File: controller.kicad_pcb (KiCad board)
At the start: 2 copper layers, 57 x 122 mm, 150 parts, among them J1 KYCON_KPJX-4S-S, J10 MicroFit_2x04, J11 JST_S4B-XH, J12 MicroFit_2x04, J13 JST_B2B-XH, J14 JST_S2B-XH, J16 MLX_1x03, J17 MLX_1x03, J2 MicroFit_2x02, J3 24V/5A OUT, J4 DB25 FEMALE, J5 JST_S6B-XH, J6 JST_S4B-XH, J7 MicroFit_2x04, J8 JST_S4B-XH, J9 JST_S4B-XH, K1 TE_OJS_24V_10A, Q1 BC847, Q2 IRF9540SPBF, Q3 BC857, Q4 BC847, Q5 BC857, U1 MC78M12CDT-TR, U2 MAX5035BUSA, U3 LM358EDR2G, U4 74HC245, U5 74HC245, U6 ACSL-6310, U7 ACSL-6310

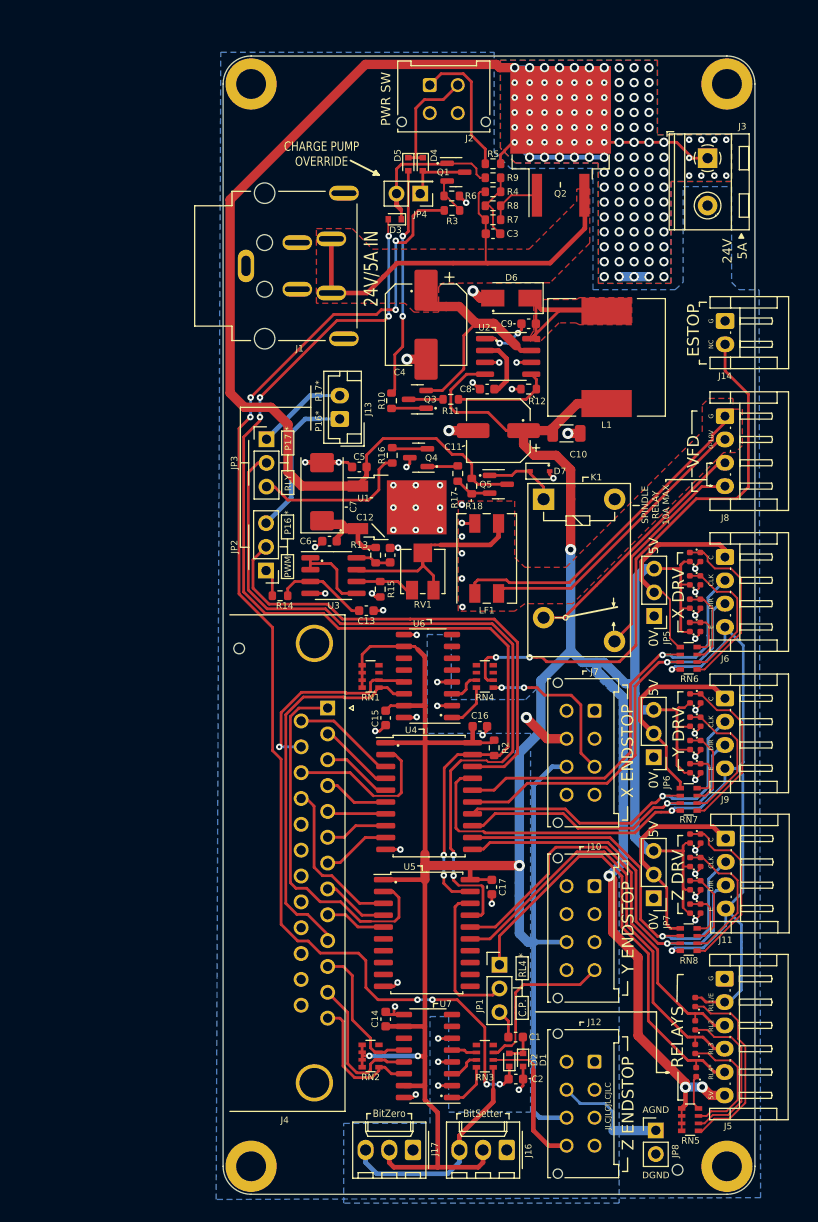
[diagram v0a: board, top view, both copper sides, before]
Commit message: Fixed yesterday's fix. Changed relay layout to allow 3A max terminal current, actually. Also changed VFD 0-10V PCB Farraday shield to reference VFD AGND instead of local GND.
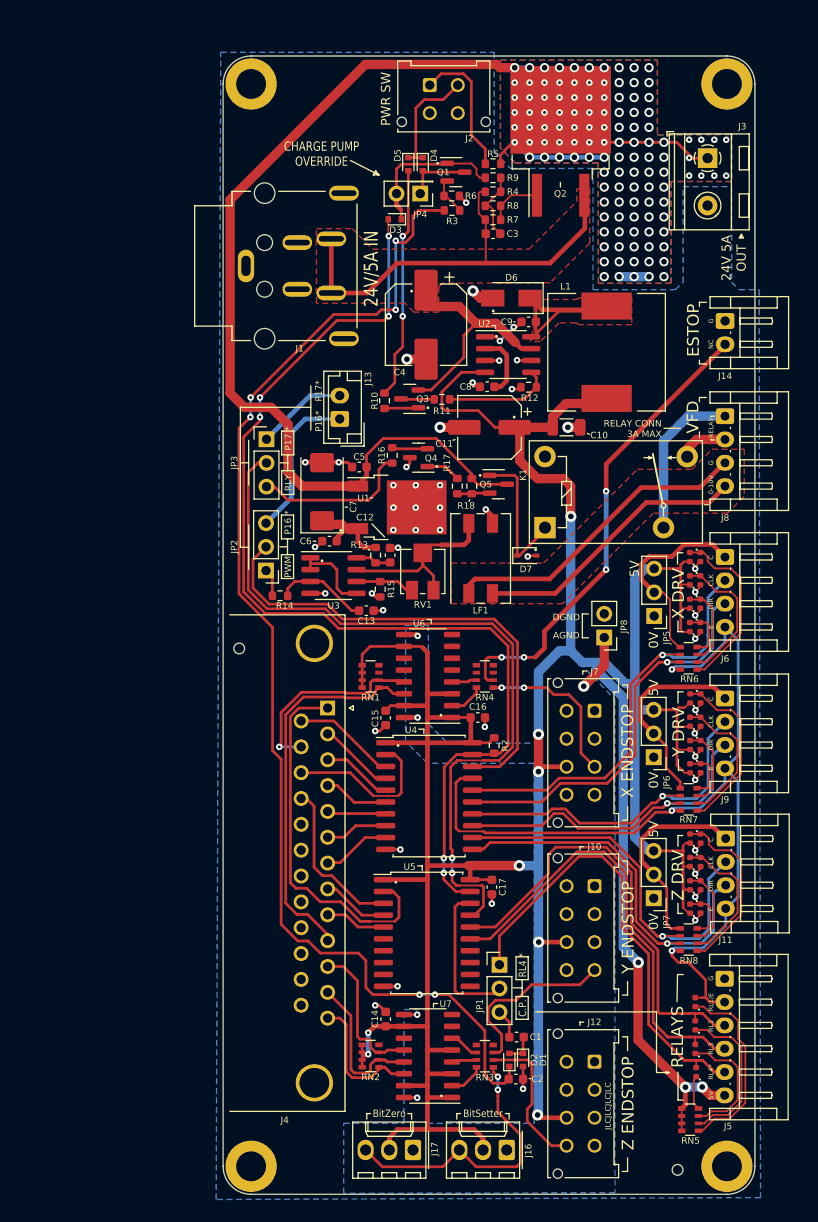
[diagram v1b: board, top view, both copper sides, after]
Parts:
- removed NT24: DNI, -Project:NetTie-2_SMD_Pad1.0mm
- K1: value TE_OJS_24V_10A -> OJS-SH-124HMF
- NT21: footprint -Project:NetTie-2_SMD_Pad0.3mm -> -Project:NetTie-2_SMD_Pad1.0mm; moved to B.Cu
- NT22: footprint -Project:NetTie-2_SMD_Pad0.3mm -> -Project:NetTie-2_SMD_Pad1.0mm
- NT23: footprint -Project:NetTie-2_SMD_Pad0.3mm -> -Project:NetTie-2_SMD_Pad0.5mm
- NT7: moved to F.Cu
- moved JP8 53.1 mm to (117.4, 111.3), turned to 180 degrees
- moved NT22 19.1 mm to (128.0, 90.1), turned to 0 degrees
- moved D7 9.16 mm to (109.1, 102.5)
- moved NT7 6.71 mm to (125.7, 146.2), turned to 0 degrees
- moved NT10 6.49 mm to (113.8, 148.6), turned to 0 degrees
- moved NT21 5.22 mm to (123.8, 96.8), turned to 90 degrees
- moved K1 3.05 mm to (111.0, 99.5), turned to 0 degrees
- moved R17 1.35 mm to (101.7, 95.1)
- moved NT12 1.35 mm to (106.0, 160.8)
- moved C11 1.01 mm to (105.1, 88.8)
- moved C16 0.97 mm to (103.8, 119.9)
- moved R11 0.95 mm to (100.0, 85.8)
- moved Q3 0.82 mm to (96.5, 85.8)
- moved NT13 0.75 mm to (109.7, 113.5)
- moved R10 0.75 mm to (93.8, 86.0)
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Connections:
- J10 pad 7: Net-(J10-Pad7) -> +5V
- J12 pad 7: Net-(J10-Pad7) -> +5V
- J7 pad 7: Net-(J10-Pad7) -> +5V
- J8 pad 1: /Connectors/DGND -> /Connectors/VFD_FWD
- J8 pad 2: /Connectors/0-10V -> /Connectors/VFD_XGND
- J8 pad 3: /Connectors/XGND -> /Connectors/VFD_0-10V
- J8 pad 4: /Connectors/FWD -> /Connectors/VFD_AGND
- K1 pad 3: /Connectors/SPNDL_RELAY_NO -> /Connectors/SPNDL_RELAY_COM
- K1 pad 5: /Connectors/SPNDL_RELAY_COM -> /Connectors/SPNDL_RELAY_NO
- LF1 pad 1: /Connectors/DGND -> /Connectors/VFD_0-10V
- LF1 pad 2: /Connectors/0-10V -> /Connectors/VFD_AGND
- LF1 pad 3: Net-(LF1-Pad3) -> GND
- LF1 pad 4: GND -> Net-(LF1-Pad4)
- NT21 pad 2: /Connectors/FWD -> /Connectors/VFD_FWD
- NT22 pad 2: /Connectors/XGND -> /Connectors/VFD_XGND
- NT23 pad 2: Net-(LF1-Pad3) -> Net-(LF1-Pad4)
- RN3 pad 2: Net-(RN3-Pad2) -> Net-(U7-Pad6)
- RN3 pad 3: Net-(RN3-Pad3) -> Net-(U7-Pad4)
- U6 pad 1: Net-(RN4-Pad8) -> +5V
- U6 pad 16: GND -> GNDA
- U6 pad 2: GNDA -> Net-(RN4-Pad8)
- U6 pad 3: Net-(RN4-Pad7) -> +5V
- U6 pad 4: GNDA -> Net-(RN4-Pad7)
- U6 pad 9: GND -> GNDA
- U7 pad 1: Net-(RN3-Pad4) -> +5V
- U7 pad 16: GND -> GNDA
- U7 pad 2: GNDA -> Net-(RN3-Pad4)
- U7 pad 3: Net-(RN3-Pad3) -> +5V
- U7 pad 4: GNDA -> Net-(U7-Pad4)
- U7 pad 5: Net-(RN3-Pad2) -> +5V
- U7 pad 6: GNDA -> Net-(U7-Pad6)
- U7 pad 9: GND -> GNDA
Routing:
- net Net-(J10-Pad7): track 52.6 -> 0.00 mm
- net +5V: track 181.3 -> 229.0 mm, vias 4 -> 8
- net /Connectors/DGND: track 35.6 -> 0.00 mm
- net /Connectors/VFD_0-10V: track 0.00 -> 33.8 mm
- net /Connectors/0-10V: track 30.6 -> 0.00 mm
- net /Connectors/VFD_AGND: track 0.00 -> 29.7 mm
- net /Connectors/SPNDL_RELAY_NO: track 21.0 -> 2.05 mm
- net /Connectors/XGND: track 18.0 -> 0.00 mm
- net /Connectors/VFD_FWD: track 0.00 -> 13.5 mm
- net GNDA: track 25.5 -> 12.0 mm, vias 6 -> 5
- net /Connectors/EMRG_STOP: track 51.8 -> 42.0 mm, vias 0 -> 2
- net /Connectors/YMIN_OUT: track 5.94 -> 15.7 mm
- net /Connectors/YMIN: track 11.0 -> 2.91 mm
- net Net-(LF1-Pad3): track 8.01 -> 0.00 mm
- net Net-(D7-Pad1): track 8.12 -> 15.8 mm
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- added copper zone on F.Cu, net /Connectors/VFD_AGND
- removed copper zone on F.Cu, net GND
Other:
- board text added: "24V 5A OUT"
- board text added: "Farraday shield"
- board text added: "RELAY"
- board text added: "RELAY CONN 3A MAX"
- board text removed: "24V 5A"
- board text removed: "SPINDLE RELAY 10A MAX"

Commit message: Tidied up F.Fab and some silk screen. Added back 2 missing tooling holes.
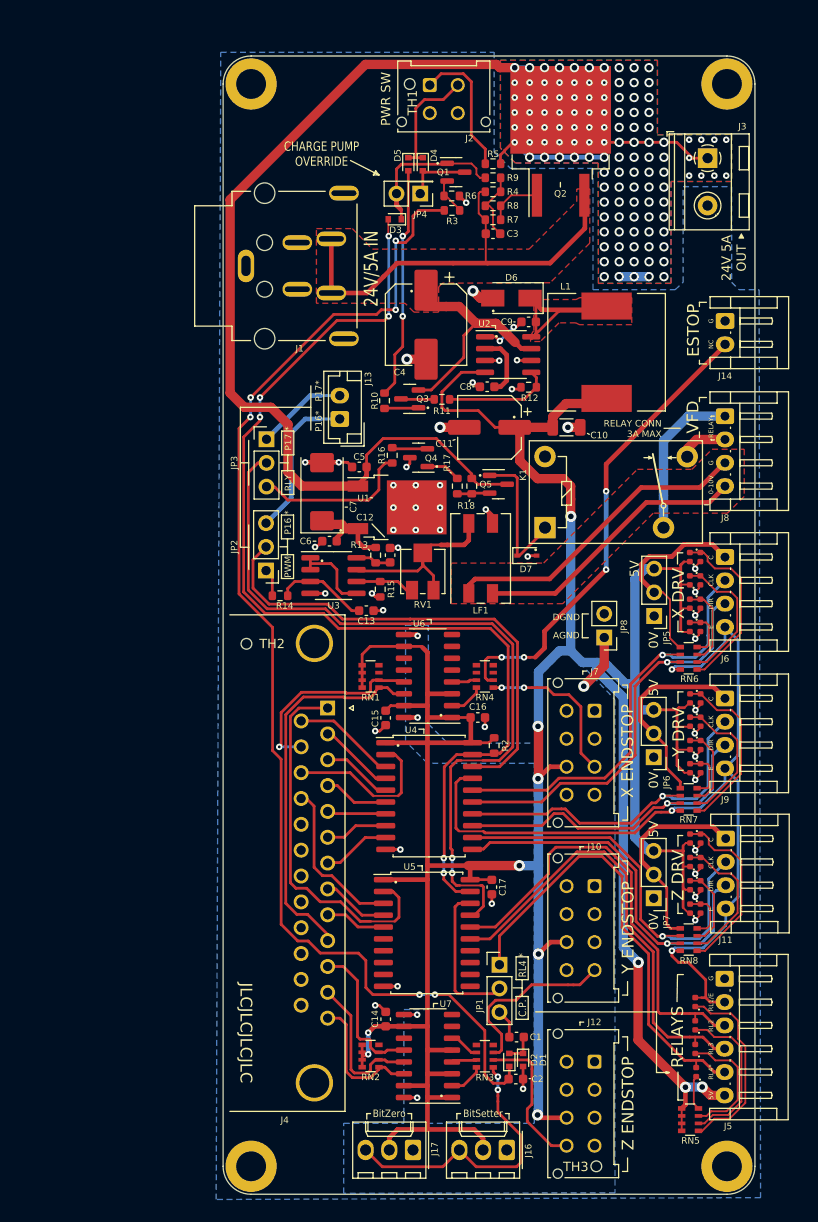
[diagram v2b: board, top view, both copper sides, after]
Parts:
- added TH1: JLC_ToolingHole, -Project:JLC_ToolingHole, F.Cu at (96.5, 52.0)
- C10: value 22u -> 22u Ceramic
- JP8: value GND_ISO -> GND/AGND ISOLATOR
- moved TH3 8.72 mm to (116.5, 168.0)
- moved TH2 0.93 mm to (79.0, 112.0)
- renumbered TH3 to TH2, TH2 to TH3
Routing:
- net +5V: track 229.0 -> 230.0 mm
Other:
- board text added: "TOOLING HOLE 1/3"
- board text added: "TOOLING HOLE 2/3"
- board text added: "TOOLING HOLE 3/3"
- board text removed: "J14"

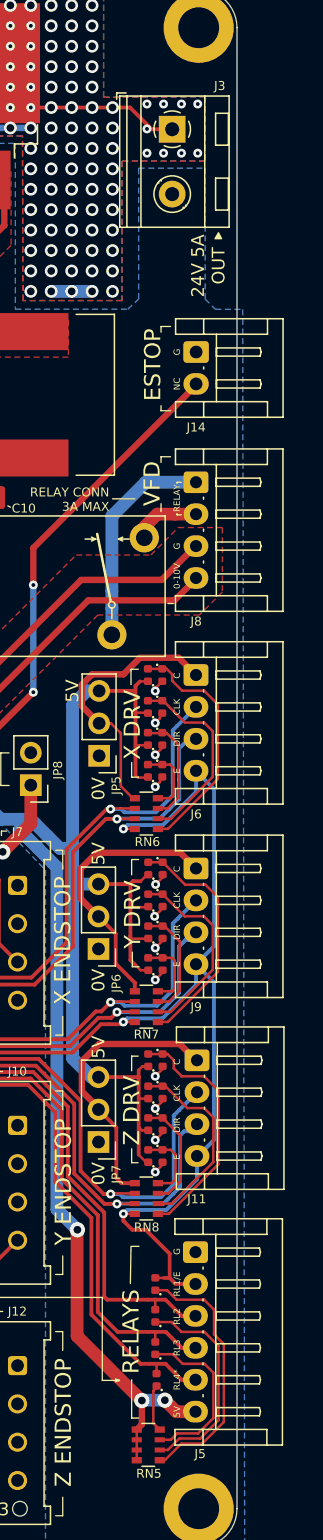
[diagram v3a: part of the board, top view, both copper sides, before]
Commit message: WIP: Changing to terminal blocks for stepper, relay and VFD ports.
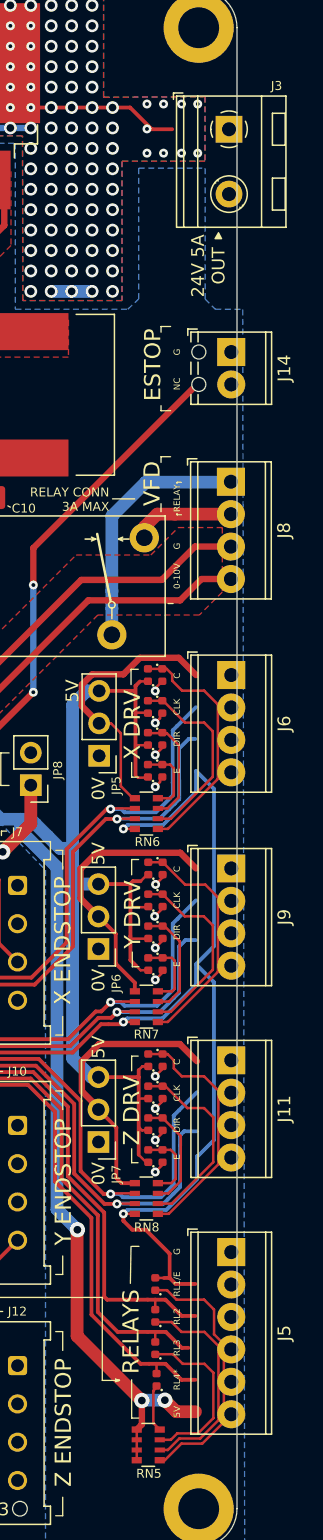
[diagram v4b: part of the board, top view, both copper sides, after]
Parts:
- J11, J6, J8, J9: footprint Connector_JST:JST_EH_S4B-EH_1x04_P2.50mm_Horizontal -> TerminalBlock_Phoenix:TerminalBlock_Phoenix_MPT-0,5-4-2.54_1x04_P2.54mm_Horizontal
- J14: footprint Connector_JST:JST_EH_S2B-EH_1x02_P2.50mm_Horizontal -> TerminalBlock_Phoenix:TerminalBlock_Phoenix_MPT-0,5-2-2.54_1x02_P2.54mm_Horizontal
- J5: footprint Connector_JST:JST_EH_S6B-EH_1x06_P2.50mm_Horizontal -> TerminalBlock_Phoenix:TerminalBlock_Phoenix_MPT-0,5-6-2.54_1x06_P2.54mm_Horizontal
- moved J3 4.45 mm to (132.9, 60.0)
- moved J5 2.80 mm to (133.1, 147.9)
- moved J6 2.76 mm to (133.1, 102.7)
- moved J9 2.76 mm to (133.1, 117.8)
- moved J14 2.75 mm to (133.1, 77.4)
- moved J8 2.74 mm to (133.1, 87.6)
- moved J11 2.68 mm to (133.1, 132.9)
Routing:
- net Net-(D11-Pad2): track 20.6 -> 0.00 mm
- net Net-(D10-Pad2): track 17.1 -> 37.7 mm
- net /Connectors/VFD_0-10V: track 33.8 -> 36.5 mm
- net /Connectors/VFD_AGND: track 29.7 -> 32.4 mm
- net /Connectors/VFD_FWD: track 13.5 -> 16.2 mm
- net /Connectors/VFD_XGND: track 1.64 -> 4.25 mm

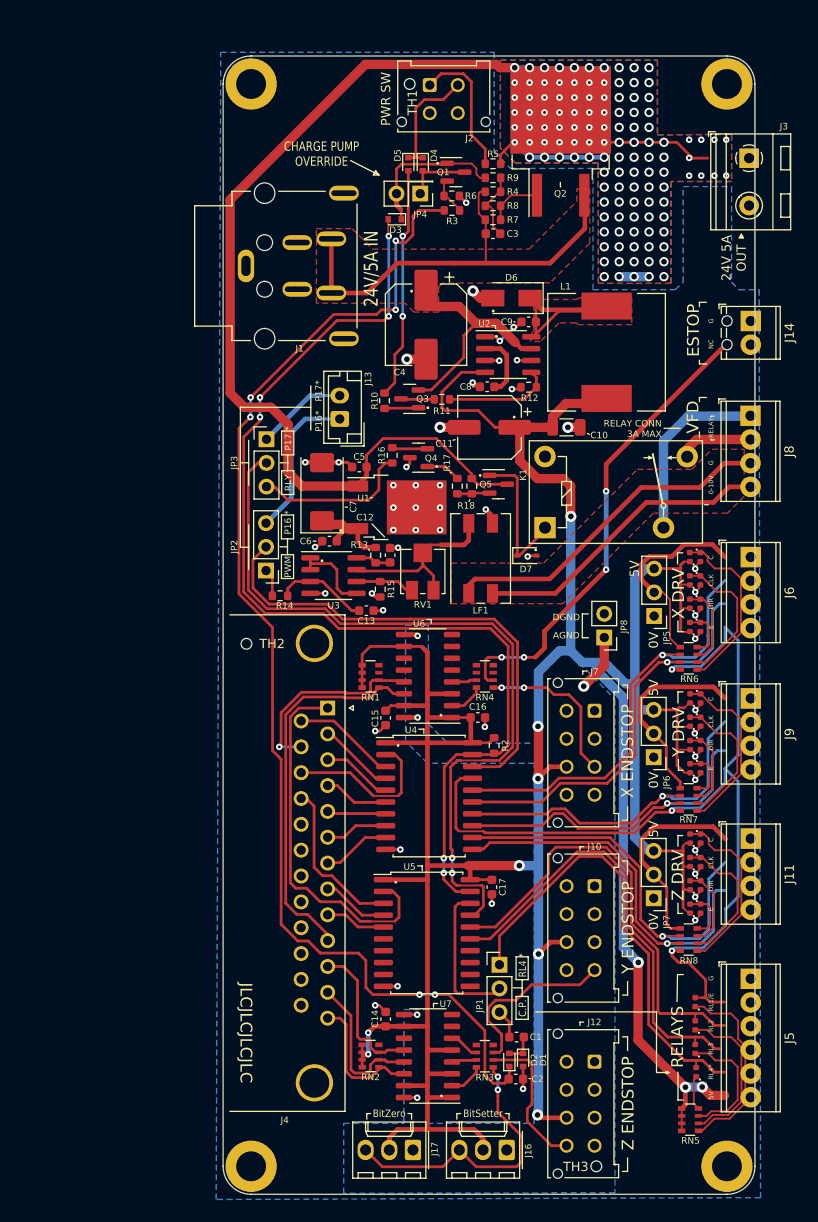
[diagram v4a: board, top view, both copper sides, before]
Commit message: Completed change to screw terminal blocks. (P16/17 remains JST.)
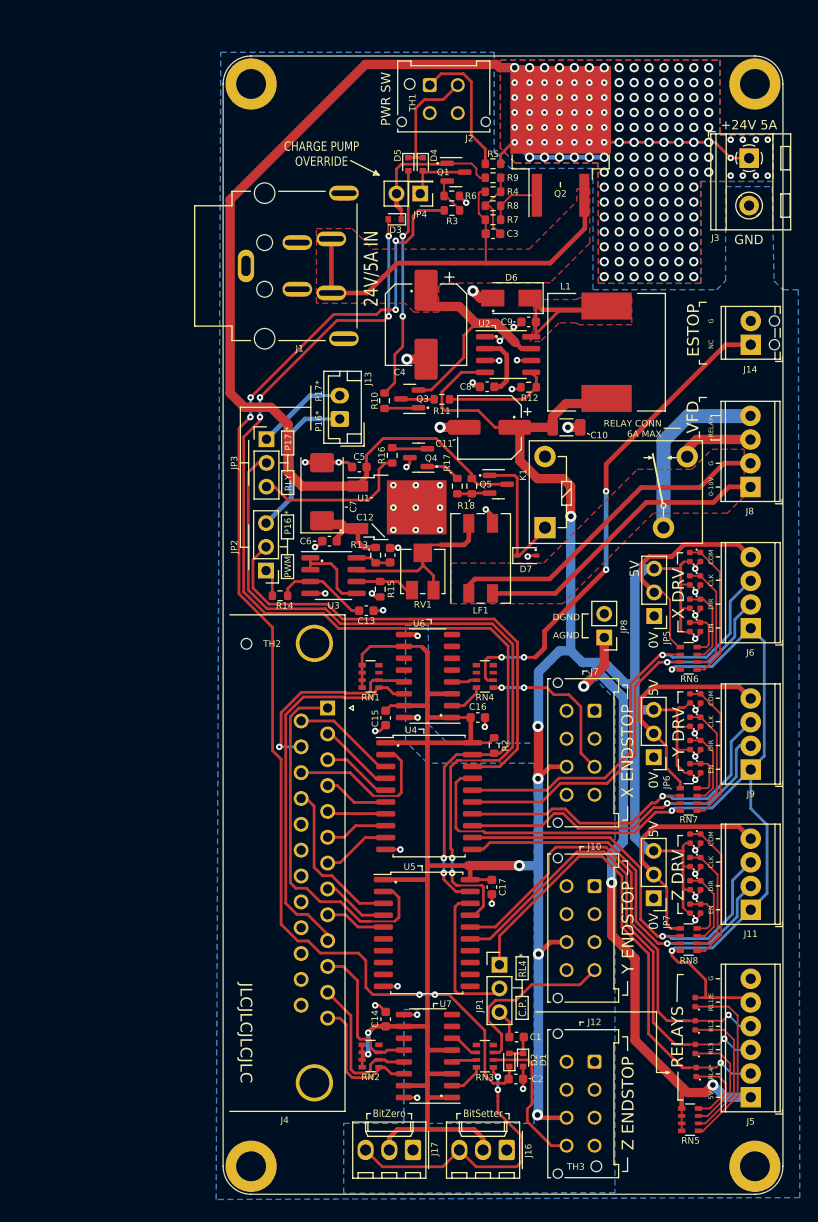
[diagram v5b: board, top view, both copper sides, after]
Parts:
- NT21: footprint -Project:NetTie-2_SMD_Pad1.0mm -> -Project:NetTie-2_SMD_Pad1.5mm
- moved J5 12.7 mm to (133.1, 160.6), turned to 90 degrees
- moved J9 7.63 mm to (133.1, 125.5), turned to 90 degrees
- moved J11 7.63 mm to (133.1, 140.5), turned to 90 degrees
- moved J6 7.63 mm to (133.1, 110.3), turned to 90 degrees
- moved J8 7.63 mm to (133.1, 95.2), turned to 90 degrees
- moved NT16 6.53 mm to (128.9, 128.1)
- moved NT18 6.46 mm to (129.1, 143.1)
- moved NT14 6.45 mm to (128.8, 113.0)
- moved H2 3.00 mm to (133.6, 52.0)
- moved H4 3.00 mm to (133.6, 168.0)
- moved J14 2.54 mm to (133.1, 79.9), turned to 90 degrees
- moved NT19 1.11 mm to (129.4, 143.4)
- moved NT4 1.06 mm to (126.2, 157.4)
- moved NT5 1.00 mm to (126.2, 154.9)
- moved NT17 0.98 mm to (129.3, 128.4)
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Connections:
- J11 pad 1: /Connectors/Z_COM -> /Connectors/EN
- J11 pad 2: /Connectors/ZCLK -> /Connectors/ZDIR
- J11 pad 3: /Connectors/ZDIR -> /Connectors/ZCLK
- J11 pad 4: /Connectors/EN -> /Connectors/Z_COM
- J14 pad 1: GND -> /Connectors/EMRG_STOP
- J14 pad 2: /Connectors/EMRG_STOP -> GND
- J5 pad 1: GND -> /Connectors/RELAY_5V
- J5 pad 2: /Connectors/RELAY1 -> /Connectors/RELAY4
- J5 pad 3: /Connectors/RELAY2 -> /Connectors/RELAY3
- J5 pad 4: /Connectors/RELAY3 -> /Connectors/RELAY2
- J5 pad 5: /Connectors/RELAY4 -> /Connectors/RELAY1
- J5 pad 6: /Connectors/RELAY_5V -> GND
- J6 pad 1: /Connectors/X_COM -> /Connectors/EN
- J6 pad 2: /Connectors/XCLK -> /Connectors/XDIR
- J6 pad 3: /Connectors/XDIR -> /Connectors/XCLK
- J6 pad 4: /Connectors/EN -> /Connectors/X_COM
- J8 pad 1: /Connectors/VFD_FWD -> /Connectors/VFD_AGND
- J8 pad 2: /Connectors/VFD_XGND -> /Connectors/VFD_0-10V
- J8 pad 3: /Connectors/VFD_0-10V -> /Connectors/VFD_XGND
- J8 pad 4: /Connectors/VFD_AGND -> /Connectors/VFD_FWD
- J9 pad 1: /Connectors/Y_COM -> /Connectors/EN
- J9 pad 2: /Connectors/YCLK -> /Connectors/YDIR
- J9 pad 3: /Connectors/YDIR -> /Connectors/YCLK
- J9 pad 4: /Connectors/EN -> /Connectors/Y_COM
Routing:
- net Net-(D10-Pad2): track 37.7 -> 15.6 mm
- net Net-(D11-Pad2): track 0.00 -> 19.3 mm
- net /Connectors/YCLK: track 1.43 -> 9.13 mm
- net /Connectors/XCLK: track 1.52 -> 9.17 mm
- net /Connectors/ZCLK: track 1.42 -> 9.01 mm
- net /Connectors/ZCLK_IN: track 41.3 -> 35.3 mm
- net /Connectors/YCLK_IN: track 35.6 -> 29.7 mm
- net /Connectors/XCLK_IN: track 43.6 -> 37.8 mm
- net /Connectors/EN: track 63.7 -> 69.1 mm
- net /Connectors/RELAY_5V: track 56.1 -> 60.7 mm, vias 3 -> 2
- net Net-(D8-Pad2): track 3.73 -> 8.06 mm
- net /Connectors/RELAY3: track 3.91 -> 7.30 mm, vias 0 -> 1
- net Net-(D12-Pad2): track 19.1 -> 16.0 mm
- net Net-(D28-Pad2): track 19.2 -> 16.1 mm
- net /Connectors/RELAY4: track 4.33 -> 7.25 mm, vias 0 -> 1
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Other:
- board size 57 x 122 mm -> 60 x 122 mm
- board text added: "+24V 5A"
- board text added: "0 10"
- board text added: "RELAY CONN 6A MAX"
- board text removed: "24V 5A OUT"
- board text removed: "C"
- board text removed: "E"
- board text removed: "RELAY CONN 3A MAX"
